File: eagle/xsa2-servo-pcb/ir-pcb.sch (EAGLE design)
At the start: 7 parts, among them IC1 ATMEGA328P-AU, IC2 PL-IRM0101, IC3 PL-IRM0101, IC4 PL-IRM0101, IC5 PL-IRM0101, IC6 PL-IRM0101, IC7 PL-IRM0101

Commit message: [eagle] 部品追加
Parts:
- added JP1: (no value), pinhead:PINHD-2X3
- added JP2: (no value), pinhead:PINHD-1X6/90
- added JP3: (no value), pinhead:PINHD-2X6
- added LED1, LED2, LED3, LED4, LED5, LED6: OSI5FU5111C-40, SamacSys_Parts:OSI5FU5111C-40
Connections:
- new net +3V3: IC2.VCC, IC3.VCC, IC4.VCC, IC5.VCC, IC6.VCC, IC7.VCC, JP1.2, JP2.3
- new net GND: IC2.GND, IC3.GND, IC4.GND, IC5.GND, IC6.GND, IC7.GND, JP1.6, JP2.1, JP2.2
- new net N$1: IC1.PB4_[PCINT4], JP1.1
- new net N$2: IC1.PB3_[PCINT3], JP1.4
- new net N$3: IC1.PC6_[RESET/PCINT14], JP1.5
- new net N$4: IC1.PD4_[PCINT20], IC2.VOUT, IC3.VOUT, IC4.VOUT, IC5.VOUT, IC6.VOUT, IC7.VOUT
- new net N$5: IC1.PB5_[PCINT5], JP1.3
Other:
- moved on the sheet: IC2, IC3, IC4, IC5, IC6, IC7

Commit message: [eagle] 基板設計追加
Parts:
- added C1, C2: 0.1u, rcl:C-EUC0603
- added Q1: IRLML6402, SamacSys_Parts:IRLML6402
- added Q2, Q3, Q4: IRFML8244, SamacSys_Parts:IRFML8244
- added Q5, Q6, Q7: 2SC2712-GR_F_, SamacSys_Parts:2SC2712-GR_F_
- added R1, R6: 1k, rcl:R-US_R0603
- added R2, R3: 1, rcl:R-US_R0603
- added R4: 2, rcl:R-US_R0603
- added R5: 10, rcl:R-US_R0603
- added Y1: MA-506_8.0000M-D3__ROHS, SamacSys_Parts:MA-506_8.0000M-D3__ROHS
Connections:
- new net N$10: IC1.PD3_[PCINT19], Q1.G, R1.2
- new net N$12: LED3.K, LED6.K, R2.2, R3.2, R4.2, R5.2
- new net N$13: C2.2, IC1.AREF
- new net N$14: IC1.PC4_[PCINT12], JP3.2
- new net N$15: Q2.D, R2.1, R3.1
- new net N$16: Q3.D, R4.1
- new net N$17: Q4.D, R5.1
- new net N$18: IC1.PD5_[PCINT21], Q2.G
- new net N$19: IC1.PD6_[PCINT22], Q3.G
- new net N$20: IC1.PD7_[PCINT23], Q4.G
- new net N$21: IC1.PC5_[PCINT13], JP3.3
- new net N$22: IC1.PB6_[PCINT6], Y1.NO_1, Y1.NO_2
- new net N$23: IC1.PD0_[PCINT16], JP2.4, JP3.4
- new net N$24: IC1.PD1_[PCINT17], JP2.5, JP3.5
- new net N$25: C1.2, JP2.6
- new net N$26: IC1.PB7_[PCINT7], Y1.COIL_1, Y1.COIL_2
- new net N$4: LED1.A, LED4.A, Q1.D, R6.2
- new net N$6: LED1.K, LED2.A
- new net N$7: LED2.K, LED3.A
- new net N$8: LED4.K, LED5.A
- new net N$9: LED5.K, LED6.A
- new net VDD: JP3.12, Q1.S, R1.1
- net +3V3: now also IC1.AVCC, IC1.VCC_1, IC1.VCC_2, JP3.7
- net GND: now also C2.1, IC1.GND_1, IC1.GND_2, IC1.GND_3, JP3.1, Q2.S, Q3.S, Q4.S, R6.1
- net N$3: now also C1.1, JP3.6
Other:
- moved on the sheet: IC2, IC3, IC4, IC5, IC6, IC7, JP1, JP3, LED1, LED2, LED3, LED4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

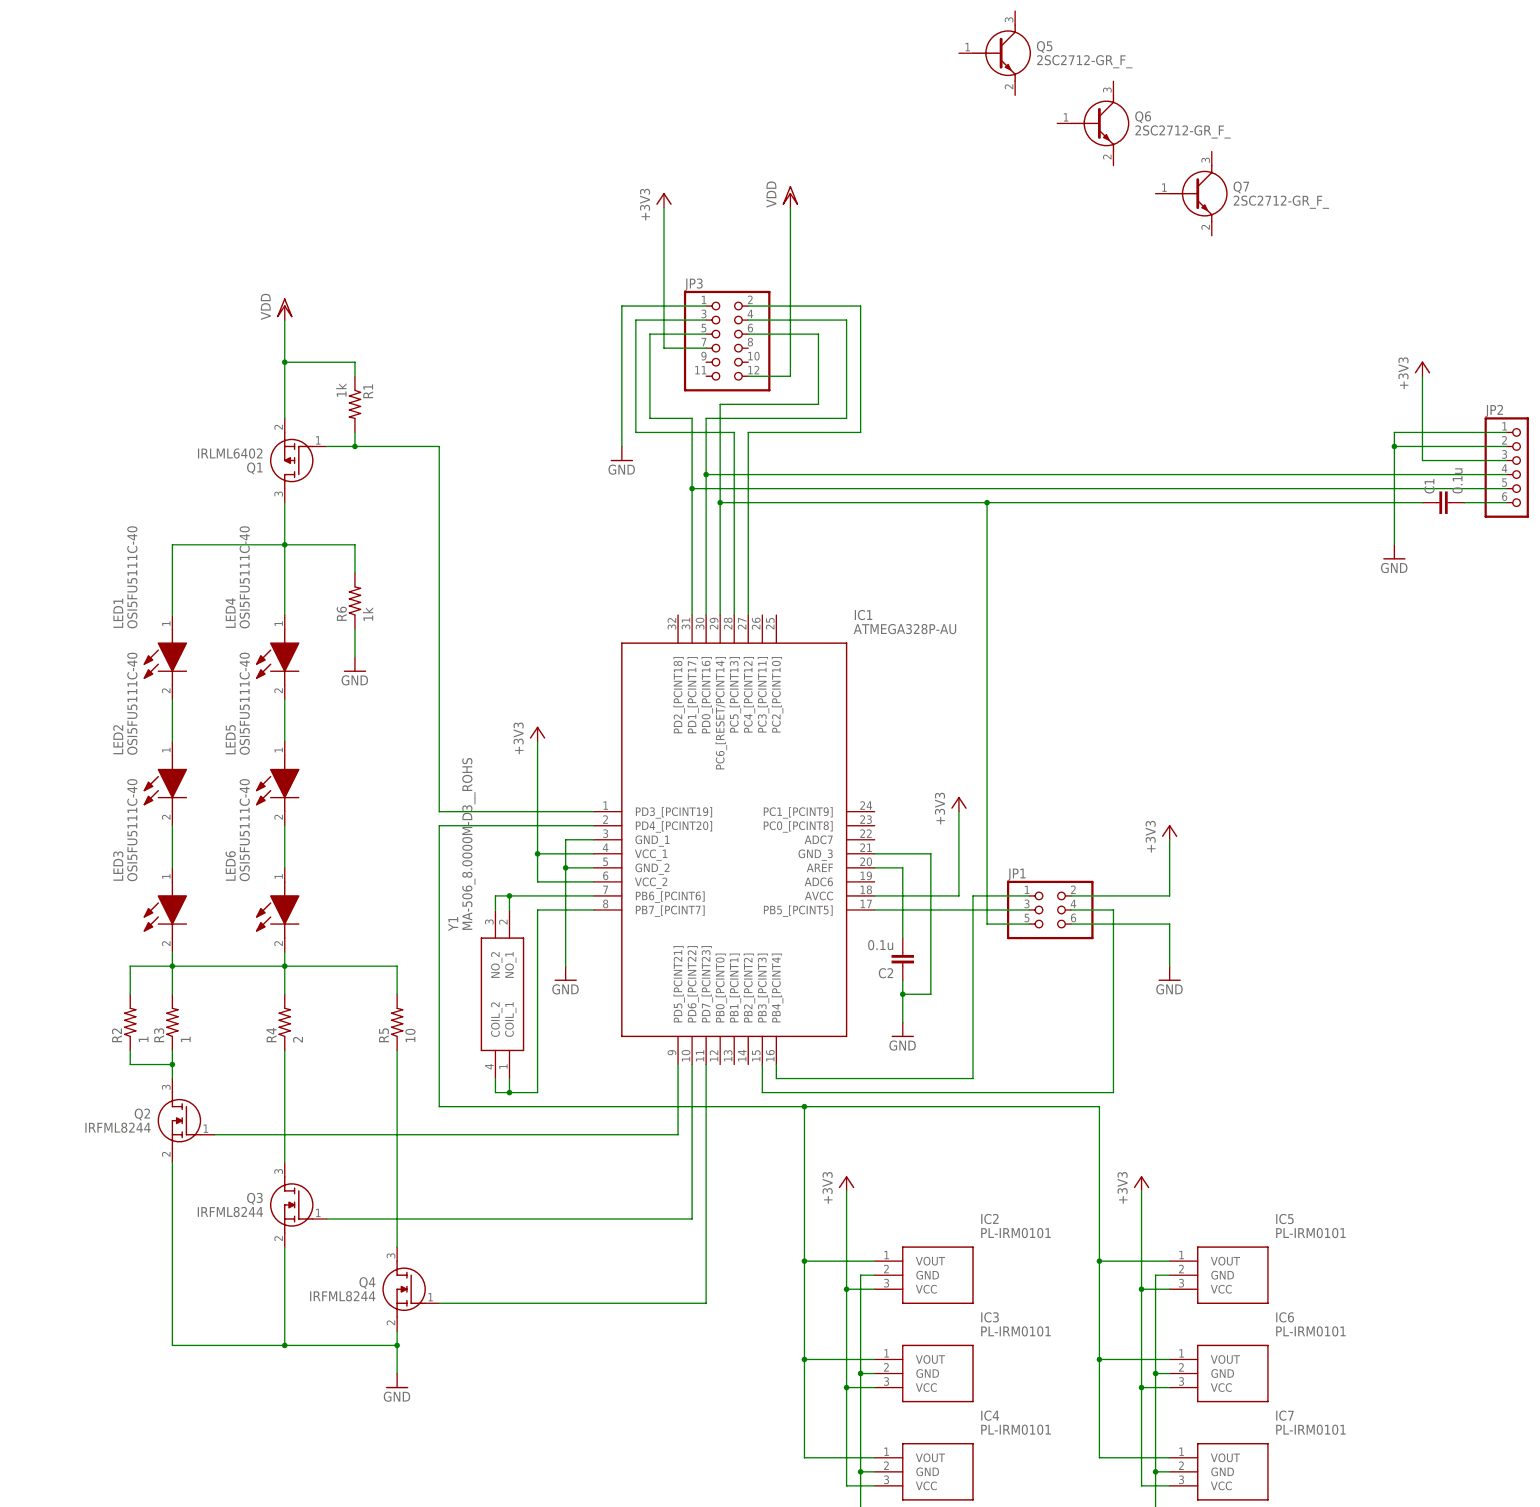
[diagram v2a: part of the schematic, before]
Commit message: [eagle] 回路追加
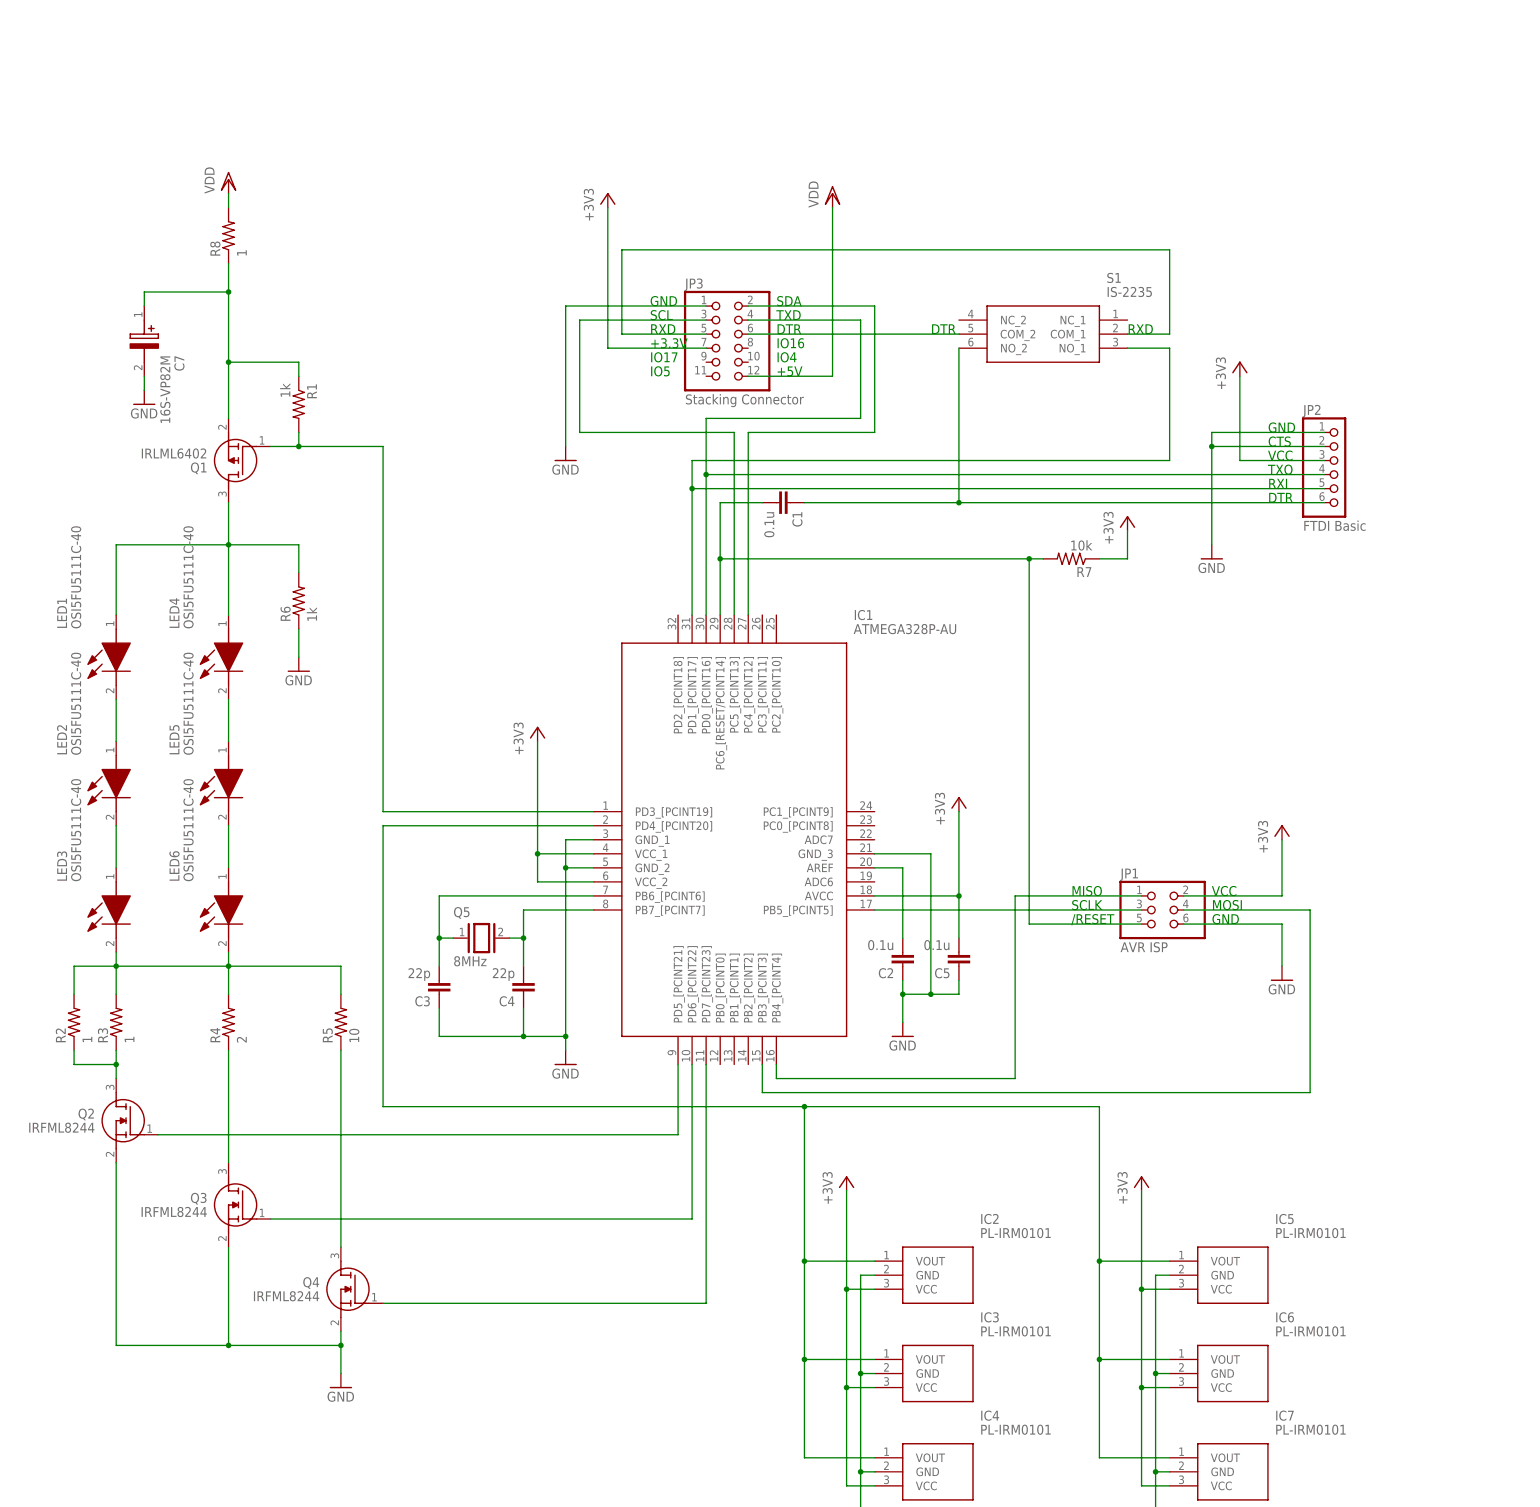
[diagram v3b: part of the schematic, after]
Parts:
- removed Q6, Q7: 2SC2712-GR_F_, SamacSys_Parts:2SC2712-GR_F_
- removed Y1: MA-506_8.0000M-D3__ROHS, SamacSys_Parts:MA-506_8.0000M-D3__ROHS
- added C3, C4: 22p, rcl:C-EUC0603
- added C5: 0.1u, rcl:C-EUC0603
- added C7: 16S-VP82M, SamacSys_Parts:16S-VP82M
- added R7: 10k, rcl:R-US_R0603
- added R8: 1, rcl:R-US_R0603
- added S1: IS-2235, SamacSys_Parts:IS-2235
- JP1: value (none) -> AVR ISP
- JP2: value (none) -> FTDI Basic
- JP3: value (none) -> Stacking Connector
- Q5: value 2SC2712-GR_F_ -> 8MHz; device SamacSys_Parts:2SC2712-GR_F_ -> special:XTAL/S
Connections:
- new net N$27: C7.+, Q1.S, R1.1, R8.1
- new net N$28: C1.1, JP2.6, S1.NO_2
- new net N$29: JP3.5, S1.COM_1
- net +3V3: now also C5.2, R7.1
- net GND: now also C3.1, C4.1, C5.1, C7.-
- net N$22: now also C3.2, Q5.1; no longer Y1.NO_1, Y1.NO_2
- net N$24: now also S1.NO_1; no longer JP3.5
- net N$25: now also IC1.PC6_[RESET/PCINT14], JP1.5, R7.2; no longer JP2.6
- net N$26: now also C4.2, Q5.2; no longer Y1.COIL_1, Y1.COIL_2
- net N$3: now also S1.COM_2; no longer C1.1, IC1.PC6_[RESET/PCINT14], JP1.5
- net VDD: now also R8.2; no longer Q1.S, R1.1
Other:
- note added: "+3.3V"
- note added: "+5V"
- note added: "/RESET"
- note added: "CTS"
- note added: "DTR"
- note added: "GND"
- note added: "IO16"
- note added: "IO17"
- note added: "IO4"
- note added: "IO5"
- note added: "MISO"
- note added: "MOSI"
- note added: "RXD"
- note added: "RXI"
- note added: "SCL"
- note added: "SCLK"
- note added: "SDA"
- note added: "TXD"
- note added: "TXO"
- note added: "VCC"
- moved on the sheet: C1, JP1, JP2, LED1, LED2, LED3, LED4, LED5, LED6, Q1, Q2, Q3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

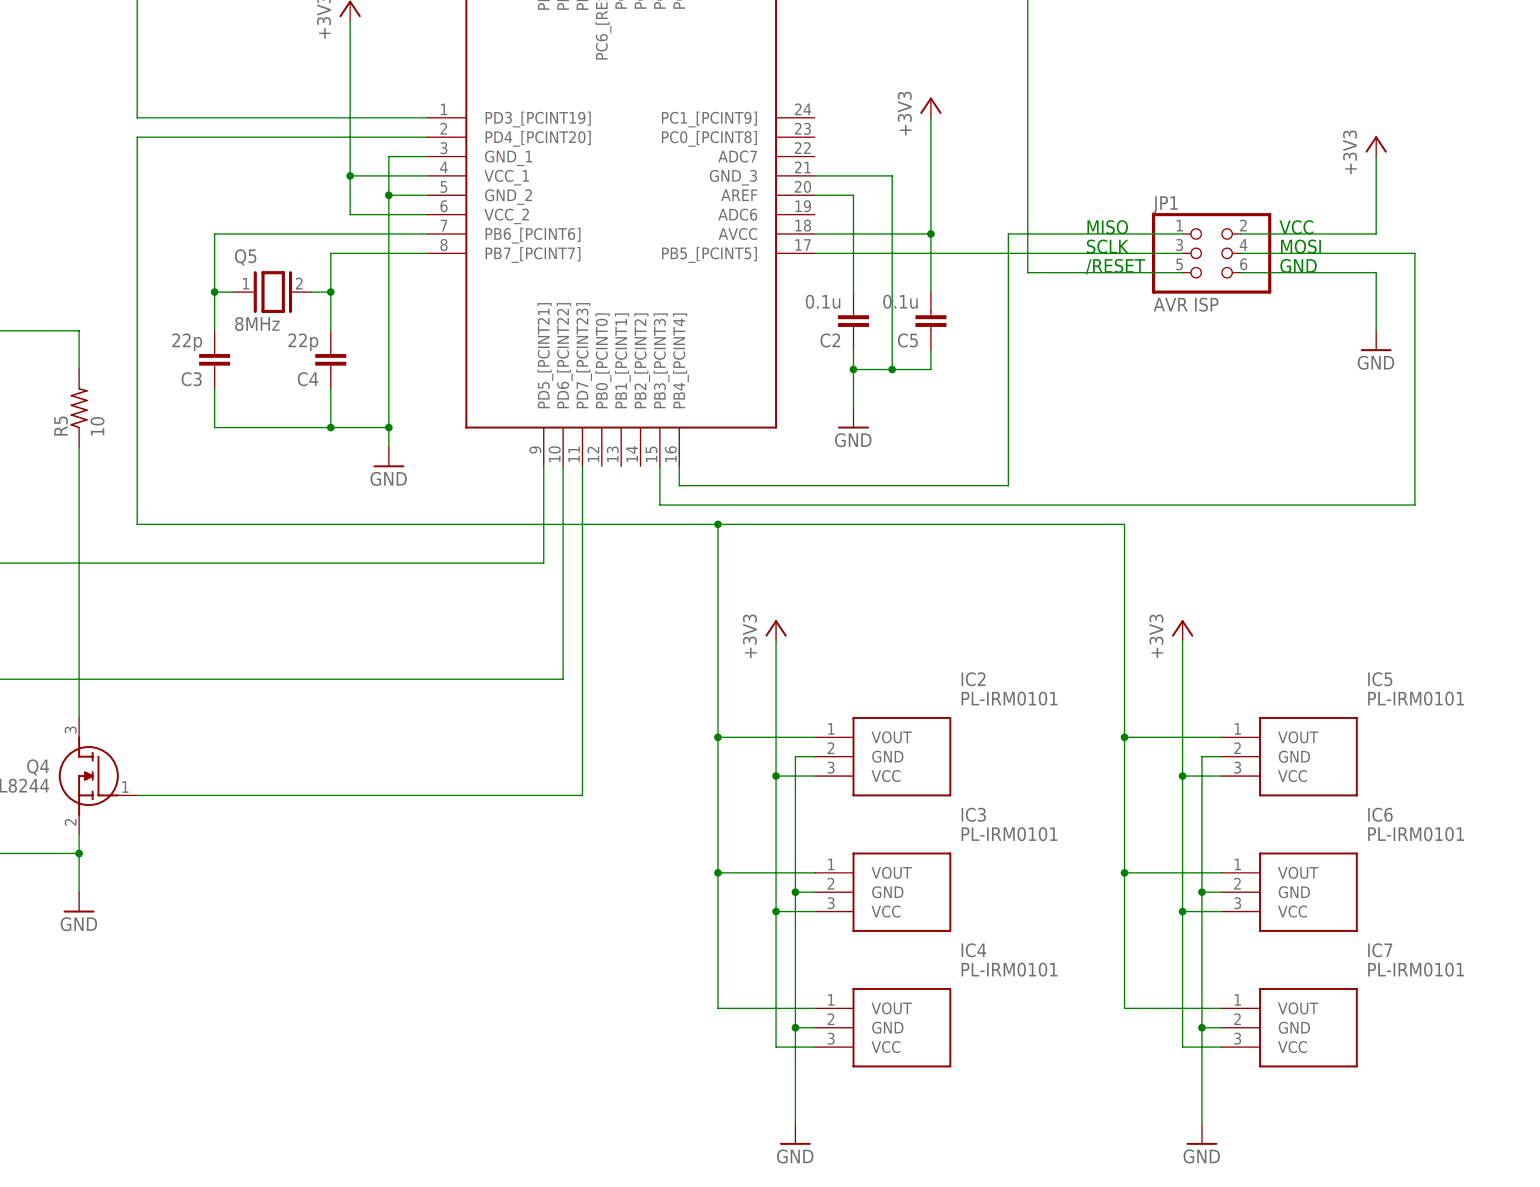
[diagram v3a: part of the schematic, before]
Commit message: [eagle] AVRの赤外受光ピンを変更
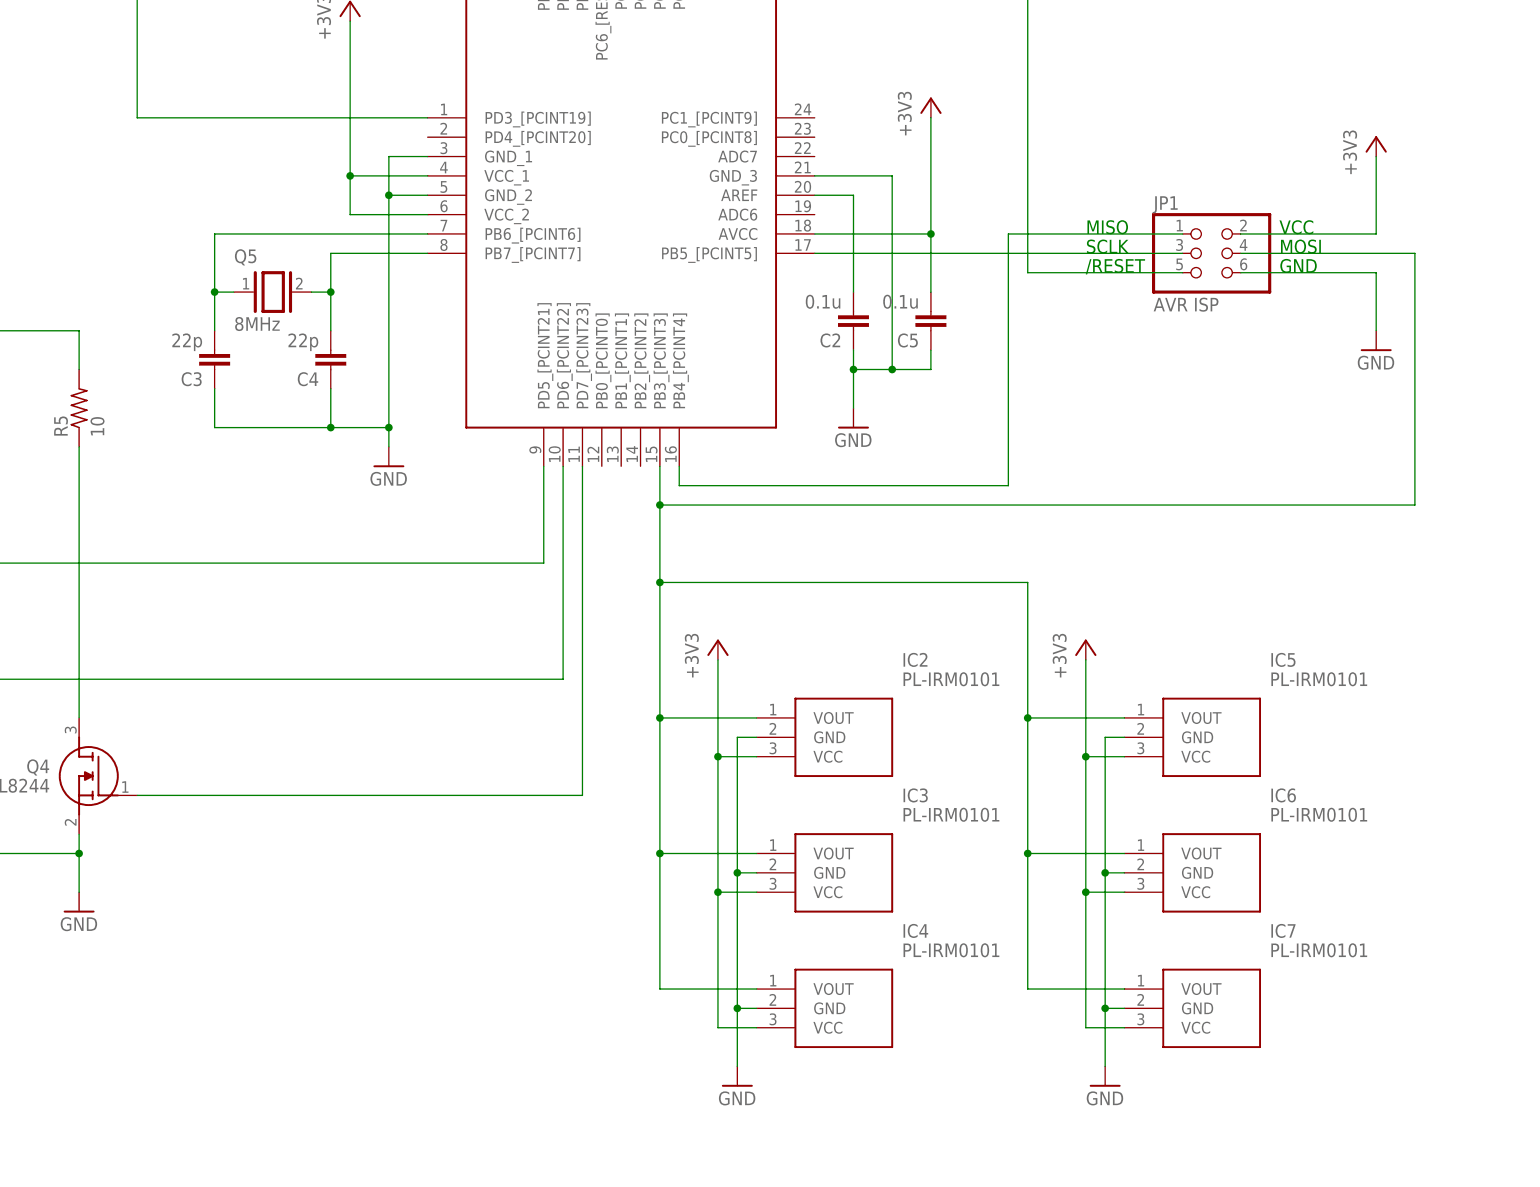
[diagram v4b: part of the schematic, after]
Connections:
- removed net N$2: IC1.PB3_[PCINT3], JP1.4
- net N$11: now also IC1.PB3_[PCINT3], JP1.4; no longer IC1.PD4_[PCINT20]
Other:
- moved on the sheet: IC2, IC3, IC4, IC5, IC6, IC7
